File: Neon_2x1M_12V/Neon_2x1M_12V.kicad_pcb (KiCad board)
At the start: 2 copper layers, 77.5 x 51.5 mm, 47 parts, among them J2 Barrel_Jack_MountingPin, J4 Barrel_Jack_MountingPin, J5 Barrel_Jack_MountingPin, J6 Conn_01x03_Pin, Q1 IRLML2502TRPBF, Q2 IRLML2502TRPBF, Q3 BSS138, Q4 BSS138, Q5 BSS138, SW1 SW_Push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

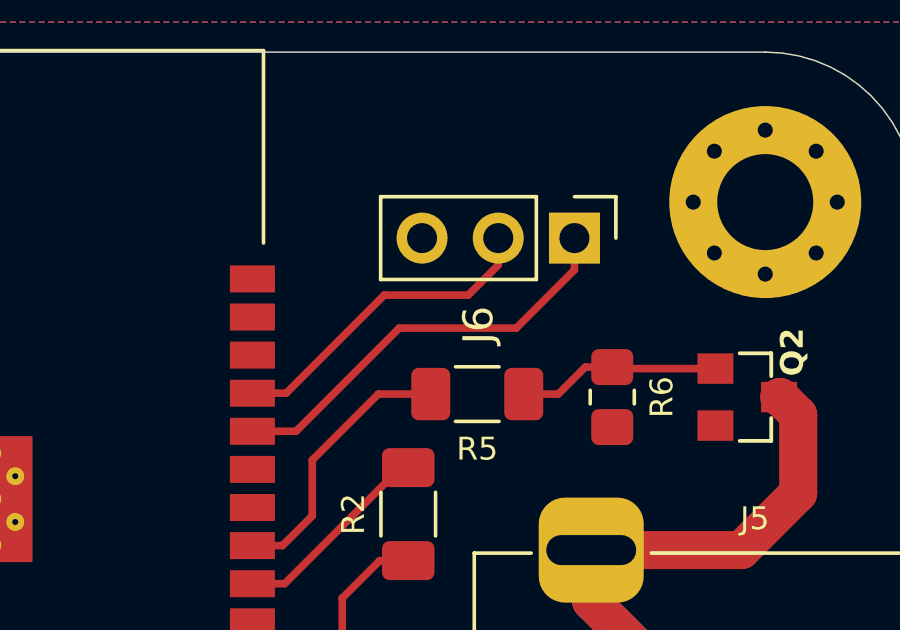
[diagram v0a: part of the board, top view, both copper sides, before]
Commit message: updated jst connector placement
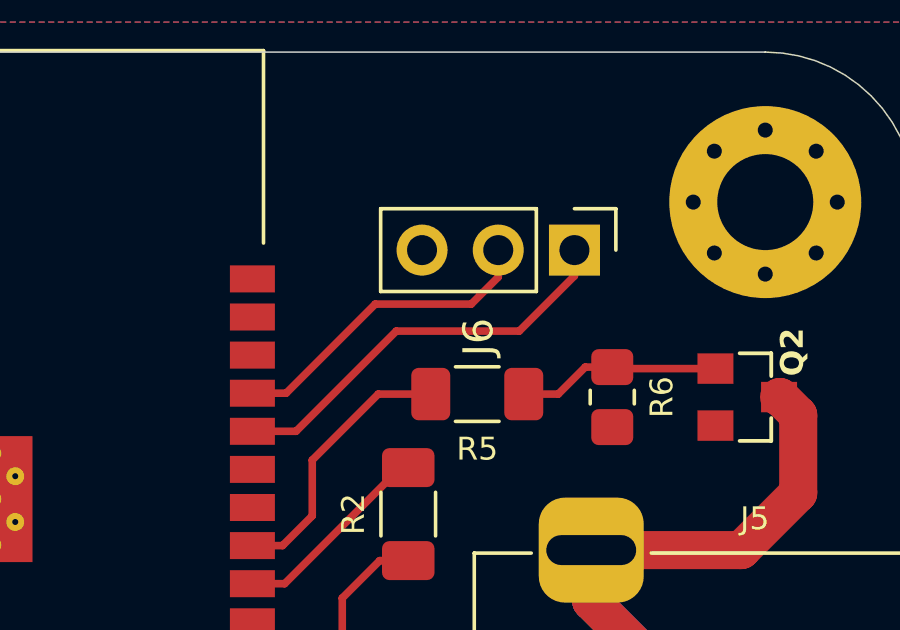
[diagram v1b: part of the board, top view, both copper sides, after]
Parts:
- moved J6 0.40 mm to (175.1, 36.6)
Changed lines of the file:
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@@
 	(footprint "Connector_PinHeader_2.54mm:PinHeader_1x03_P2.54mm_Vertical"
 		(layer "F.Cu")
-		(at 175.14 36.2 -90)
+		(at 175.14 36.6 -90)
 		(descr "Through hole straight pin header, 1x03, 2.54mm pitch, single row")
 		(tags "Through hole pin header THT 1x03 2.54mm single row")
@@
 	)
 	(segment
-		(start 171.6 38.1)
-		(end 172.6 37.1)
+		(start 168.5 38.4)
+		(end 171.7 38.4)
 		(width 0.254)
 		(layer "F.Cu")
@@
 	)
 	(segment
-		(start 168.8 38.1)
-		(end 171.6 38.1)
+		(start 164.405 41.37)
+		(end 165.53 41.37)
 		(width 0.254)
 		(layer "F.Cu")
@@
 	)
 	(segment
-		(start 172.6 37.1)
-		(end 172.6 36.2)
+		(start 171.7 38.4)
+		(end 172.6 37.5)
 		(width 0.254)
 		(layer "F.Cu")
@@
 	)
 	(segment
-		(start 164.405 41.37)
-		(end 165.53 41.37)
+		(start 165.53 41.37)
+		(end 168.5 38.4)
 		(width 0.254)
 		(layer "F.Cu")
@@
 	)
 	(segment
-		(start 165.53 41.37)
-		(end 168.8 38.1)
+		(start 172.6 37.5)
+		(end 172.6 36.6)
 		(width 0.254)
 		(layer "F.Cu")
@@
 	)
 	(segment
-		(start 169.3 39.2)
-		(end 165.86 42.64)
+		(start 173.3 39.3)
+		(end 169.2 39.3)
 		(width 0.254)
 		(layer "F.Cu")
@@
 	)
 	(segment
-		(start 175.14 37.26)
-		(end 173.2 39.2)
+		(start 175.14 37.46)
+		(end 173.3 39.3)
 		(width 0.254)
 		(layer "F.Cu")
@@
 	)
 	(segment
-		(start 165.86 42.64)
-		(end 164.405 42.64)
+		(start 169.2 39.3)
+		(end 165.86 42.64)
 		(width 0.254)
 		(layer "F.Cu")
@@
 	)
 	(segment
-		(start 173.2 39.2)
-		(end 169.3 39.2)
+		(start 165.86 42.64)
+		(end 164.405 42.64)
 		(width 0.254)
 		(layer "F.Cu")
@@
 	)
 	(segment
-		(start 175.14 36.2)
-		(end 175.14 37.26)
+		(start 175.14 36.6)
+		(end 175.14 37.46)
 		(width 0.254)
 		(layer "F.Cu")

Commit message: updated switching pin (3) the mounting pin to be unconnected as it is not important
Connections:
- J2 pad 3: GND -> (no net)
- J4 pad 3: B_Jack -> (no net)
- J5 pad 3: P_Jack -> (no net)
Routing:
- net P_Jack: track 23.1 -> 19.4 mm, vias 0 -> 1
- net B_Jack: track 31.8 -> 30.3 mm, vias 0 -> 3
